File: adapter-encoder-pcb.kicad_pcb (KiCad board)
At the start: 4 copper layers, 14 x 15.6 mm, 33 parts, among them IC1 THVD2410VDRCR, M1 THRU_HOLE_PAD, M2 THRU_HOLE_PAD, U1 TLE5009E1000FUMA1, U2 STM32G031G6U6, U3 DF52-4S-0.8H(21), U4 SPX3819M5-L-3-3, U5 C2901617, U6 DF52-4S-0.8H(21), U7 SPX3819M5-L-3-3

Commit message: curves
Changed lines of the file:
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@@
   (segment (start 143.72885 110.81185) (end 144.098724 111.181724) (width 0.25) (layer "B.Cu") (net 22))
   (segment (start 143.727448 110.81185) (end 143.72885 110.81185) (width 0.25) (layer "B.Cu") (net 22))
-  (segment (start 145.304448 116.637448) (end 145.304448 116.350474) (width 0.3048) (layer "F.Cu") (net 23))
-  (segment (start 149.376423 115.340473) (end 150.864274 113.852622) (width 0.3048) (layer "F.Cu") (net 23))
+  (segment (start 150.529448 110.362448) (end 150.104448 110.362448) (width 0.3048) (layer "F.Cu") (net 23))
   (segment (start 144.504448 107.562448) (end 144.979108 108.037108) (width 0.3048) (layer "F.Cu") (net 23))
-  (segment (start 150.529448 110.362448) (end 150.104448 110.362448) (width 0.3048) (layer "F.Cu") (net 23))
   (segment (start 150.004448 110.262448) (end 150.104448 110.362448) (width 0.3048) (layer "F.Cu") (net 23))
+  (segment (start 145.490435 115.901461) (end 145.493461 115.898435) (width 0.3048) (layer "F.Cu") (net 23))
   (segment (start 145.942474 115.712448) (end 148.478397 115.712448) (width 0.3048) (layer "F.Cu") (net 23))
   (segment (start 144.979108 108.037108) (end 144.979108 108.760448) (width 0.3048) (layer "F.Cu") (net 23))
-  (segment (start 145.490435 115.901461) (end 145.493461 115.898435) (width 0.3048) (layer "F.Cu") (net 23))
   (segment (start 150.864273 110.697273) (end 150.529448 110.362448) (width 0.3048) (layer "F.Cu") (net 23))
   (segment (start 148.454448 110.437448) (end 149.279448 110.437448) (width 0.2032) (layer "F.Cu") (net 23))
   (segment (start 150.004448 109.712448) (end 150.004448 110.262448) (width 0.3048) (layer "F.Cu") (net 23))
+  (segment (start 149.376423 115.340473) (end 150.120325 114.596571) (width 0.3048) (layer "F.Cu") (net 23))
   (segment (start 144.504448 106.637448) (end 144.504448 107.562448) (width 0.3048) (layer "F.Cu") (net 23))
   (segment (start 149.279448 110.437448) (end 150.029448 110.437448) (width 0.2032) (layer "F.Cu") (net 23))
+  (segment (start 151.236248 111.902494) (end 151.236248 111.595299) (width 0.3048) (layer "F.Cu") (net 23))
+  (segment (start 145.304448 116.637448) (end 145.304448 116.350474) (width 0.3048) (layer "F.Cu") (net 23))
   (segment (start 150.029448 110.437448) (end 150.104448 110.362448) (width 0.2032) (layer "F.Cu") (net 23))
-  (segment (start 151.236248 112.954597) (end 151.236248 111.595299) (width 0.3048) (layer "F.Cu") (net 23))
   (via (at 144.979108 108.760448) (size 0.45) (drill 0.2) (layers "F.Cu" "B.Cu") (net 23))
   (via (at 150.004448 109.712448) (size 0.45) (drill 0.2) (layers "F.Cu" "B.Cu") (net 23))
-  (arc (start 145.490435 115.901461) (mid 145.352784 116.10747) (end 145.304448 116.350474) (width 0.3048) (layer "F.Cu") (net 23))
+  (arc (start 145.304448 116.350474) (mid 145.352784 116.10747) (end 145.490435 115.901461) (width 0.3048) (layer "F.Cu") (net 23))
+  (arc (start 145.493461 115.898435) (mid 145.69947 115.760784) (end 145.942474 115.712448) (width 0.3048) (layer "F.Cu") (net 23))
+  (arc (start 151.236248 111.902494) (mid 150.946229 113.360518) (end 150.120325 114.596571) (width 0.3048) (layer "F.Cu") (net 23))
   (arc (start 148.478397 115.712448) (mid 148.964405 115.615775) (end 149.376423 115.340473) (width 0.3048) (layer "F.Cu") (net 23))
-  (arc (start 150.864274 113.852622) (mid 151.139575 113.440605) (end 151.236248 112.954597) (width 0.3048) (layer "F.Cu") (net 23))
-  (arc (start 150.864273 110.697273) (mid 151.139575 111.109291) (end 151.236248 111.595299) (width 0.3048) (layer "F.Cu") (net 23))
-  (arc (start 145.493461 115.898435) (mid 145.69947 115.760784) (end 145.942474 115.712448) (width 0.3048) (layer "F.Cu") (net 23))
+  (arc (start 151.236248 111.595299) (mid 151.139575 111.109291) (end 150.864273 110.697273) (width 0.3048) (layer "F.Cu") (net 23))
   (segment (start 149.605499 109.712448) (end 150.004448 109.712448) (width 0.3048) (layer "In1.Cu") (net 23))
   (segment (start 144.979108 108.760448) (end 147.601397 108.760448) (width 0.3048) (layer "In1.Cu") (net 23))

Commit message: some minor tweaks
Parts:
- moved C6 0.20 mm to (146.5, 108.6)
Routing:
- net GND: vias 19 -> 31
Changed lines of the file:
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@@
   )
   (footprint "Capacitor_SMD:C_0402_1005Metric" (layer "F.Cu")
-    (at 146.304448 108.562448 180)
+    (at 146.504448 108.562448 180)
     (descr "Capacitor SMD 0402 (1005 Metric), square (rectangular) end terminal, IPC_7351 nominal, (Body size source: IPC-SM-782 page 76, https://www.pcb-3d.com/wordpress/wp-content/uploads/ipc-sm-782a_amendment_1_and_2.pdf), generated with kicad-footprint-generator")
     (tags "capacitor")
@@
     (stroke (width 0.0254) (type solid)) (layer "Edge.Cuts"))
   (via (at 150.608848 112.037448) (size 0.45) (drill 0.2) (layers "F.Cu" "B.Cu") (net 1))
+  (via (at 144.704448 104.737448) (size 0.45) (drill 0.2) (layers "F.Cu" "B.Cu") (net 1))
   (via (at 148.379448 116.987448) (size 0.45) (drill 0.2) (layers "F.Cu" "B.Cu") (net 1))
-  (via (at 141.279448 115.037448) (size 0.45) (drill 0.2) (layers "F.Cu" "B.Cu") (net 1))
+  (via (at 141.704448 114.737448) (size 0.45) (drill 0.2) (layers "F.Cu" "B.Cu") (net 1))
   (via (at 140.929448 114.637448) (size 0.45) (drill 0.2) (layers "F.Cu" "B.Cu") (net 1))
   (via (at 141.304448 110.337448) (size 0.45) (drill 0.2) (layers "F.Cu" "B.Cu") (net 1))
   (via (at 138.954448 109.687448) (size 0.45) (drill 0.2) (layers "F.Cu" "B.Cu") (net 1))
   (via (at 149.704448 115.937448) (size 0.45) (drill 0.2) (layers "F.Cu" "B.Cu") (net 1))
+  (via (at 145.804448 118.337448) (size 0.45) (drill 0.2) (layers "F.Cu" "B.Cu") (net 1))
+  (via (at 140.004448 107.337448) (size 0.45) (drill 0.2) (layers "F.Cu" "B.Cu") (net 1))
+  (via (at 142.304448 115.237448) (size 0.45) (drill 0.2) (layers "F.Cu" "B.Cu") (net 1))
   (via (at 149.454448 114.412448) (size 0.45) (drill 0.2) (layers "F.Cu" "B.Cu") (net 1))
   (via (at 145.004448 112.937448) (size 0.45) (drill 0.2) (layers "F.Cu" "B.Cu") (net 1))
+  (via (at 143.704448 118.337448) (size 0.45) (drill 0.2) (layers "F.Cu" "B.Cu") (net 1))
   (via (at 138.704448 114.012448) (size 0.45) (drill 0.2) (layers "F.Cu" "B.Cu") (net 1))
   (via (at 149.104448 112.837448) (size 0.45) (drill 0.2) (layers "F.Cu" "B.Cu") (net 1))
-  (via (at 148.554448 113.512448) (size 0.45) (drill 0.2) (layers "F.Cu" "B.Cu") (net 1))
+  (via (at 144.704448 118.837448) (size 0.45) (drill 0.2) (layers "F.Cu" "B.Cu") (net 1))
+  (via (at 150.404448 115.037448) (size 0.45) (drill 0.2) (layers "F.Cu" "B.Cu") (net 1))
+  (via (at 148.704448 113.437448) (size 0.45) (drill 0.2) (layers "F.Cu" "B.Cu") (net 1))
   (via (at 139.940347 109.669538) (size 0.45) (drill 0.2) (layers "F.Cu" "B.Cu") (net 1))
+  (via (at 145.904448 104.537448) (size 0.45) (drill 0.2) (layers "F.Cu" "B.Cu") (net 1))
   (via (at 142.354448 108.687448) (size 0.45) (drill 0.2) (layers "F.Cu" "B.Cu") (net 1))
+  (via (at 143.704448 104.637448) (size 0.45) (drill 0.2) (layers "F.Cu" "B.Cu") (net 1))
   (via (at 138.354448 112.387448) (size 0.45) (drill 0.2) (layers "F.Cu" "B.Cu") (net 1))
   (via (at 148.454448 106.087448) (size 0.45) (drill 0.2) (layers "F.Cu" "B.Cu") (net 1))
   (via (at 138.454448 110.037448) (size 0.45) (drill 0.2) (layers "F.Cu" "B.Cu") (net 1))
-  (via (at 138.454448 113.187448) (size 0.45) (drill 0.2) (layers "F.Cu" "B.Cu") (net 1))
+  (via (at 149.904448 107.537448) (size 0.45) (drill 0.2) (layers "F.Cu" "B.Cu") (net 1))
+  (via (at 138.604448 113.137448) (size 0.45) (drill 0.2) (layers "F.Cu" "B.Cu") (net 1))
+  (via (at 150.404448 113.237448) (size 0.45) (drill 0.2) (layers "F.Cu" "B.Cu") (net 1))
+  (via (at 151.204448 110.137448) (size 0.45) (drill 0.2) (layers "F.Cu" "B.Cu") (net 1))
   (via (at 143.579448 109.662448) (size 0.45) (drill 0.2) (layers "F.Cu" "B.Cu") (net 1))
   (segment (start 144.854448 112.287448) (end 144.404448 112.287448) (width 0.25) (layer "F.Cu") (net 2))
@@
   (segment (start 145.154448 109.937448) (end 145.654448 109.937448) (width 0.254) (layer "F.Cu") (net 12))
   (segment (start 143.204448 113.912448) (end 143.204448 113.837448) (width 0.381) (layer "F.Cu") (net 12))
+  (segment (start 145.654448 109.287448) (end 146.024448 108.917448) (width 0.254) (layer "F.Cu") (net 12))
   (segment (start 145.029448 109.812448) (end 145.154448 109.937448) (width 0.254) (layer "F.Cu") (net 12))
   (segment (start 139.354448 111.537448) (end 139.504448 111.687448) (width 0.381) (layer "F.Cu") (net 12))
@@
   (segment (start 142.629448 114.162448) (end 142.629448 113.054878) (width 0.25) (layer "F.Cu") (net 12))
   (segment (start 142.791948 114.324948) (end 143.204448 113.912448) (width 0.381) (layer "F.Cu") (net 12))
-  (segment (start 145.654448 109.937448) (end 145.654448 108.732448) (width 0.254) (layer "F.Cu") (net 12))
+  (segment (start 145.654448 109.937448) (end 145.654448 109.287448) (width 0.254) (layer "F.Cu") (net 12))
   (segment (start 142.429448 112.854878) (end 142.429448 112.812448) (width 0.25) (layer "F.Cu") (net 12))
-  (segment (start 145.654448 108.732448) (end 145.824448 108.562448) (width 0.254) (layer "F.Cu") (net 12))
   (segment (start 138.504448 111.537448) (end 139.354448 111.537448) (width 0.381) (layer "F.Cu") (net 12))
+  (segment (start 146.024448 108.917448) (end 146.024448 108.562448) (width 0.254) (layer "F.Cu") (net 12))
   (segment (start 141.954448 112.537448) (end 141.954448 111.837448) (width 0.25) (layer "F.Cu") (net 12))
   (segment (start 142.629448 113.054878) (end 142.429448 112.854878) (width 0.25) (layer "F.Cu") (net 12))
@@
   (segment (start 143.727448 110.81185) (end 143.72885 110.81185) (width 0.25) (layer "B.Cu") (net 22))
   (segment (start 150.529448 110.362448) (end 150.104448 110.362448) (width 0.3048) (layer "F.Cu") (net 23))
-  (segment (start 144.504448 107.562448) (end 144.979108 108.037108) (width 0.3048) (layer "F.Cu") (net 23))
   (segment (start 150.004448 110.262448) (end 150.104448 110.362448) (width 0.3048) (layer "F.Cu") (net 23))
   (segment (start 145.490435 115.901461) (end 145.493461 115.898435) (width 0.3048) (layer "F.Cu") (net 23))
+  (segment (start 145.204448 108.762237) (end 145.204448 108.262448) (width 0.3048) (layer "F.Cu") (net 23))
   (segment (start 145.942474 115.712448) (end 148.478397 115.712448) (width 0.3048) (layer "F.Cu") (net 23))
-  (segment (start 144.979108 108.037108) (end 144.979108 108.760448) (width 0.3048) (layer "F.Cu") (net 23))
   (segment (start 150.864273 110.697273) (end 150.529448 110.362448) (width 0.3048) (layer "F.Cu") (net 23))
   (segment (start 148.454448 110.437448) (end 149.279448 110.437448) (width 0.2032) (layer "F.Cu") (net 23))
   (segment (start 150.004448 109.712448) (end 150.004448 110.262448) (width 0.3048) (layer "F.Cu") (net 23))
   (segment (start 149.376423 115.340473) (end 150.120325 114.596571) (width 0.3048) (layer "F.Cu") (net 23))
-  (segment (start 144.504448 106.637448) (end 144.504448 107.562448) (width 0.3048) (layer "F.Cu") (net 23))
+  (segment (start 145.204448 108.262448) (end 144.504448 107.562448) (width 0.3048) (layer "F.Cu") (net 23))
   (segment (start 149.279448 110.437448) (end 150.029448 110.437448) (width 0.2032) (layer "F.Cu") (net 23))
   (segment (start 151.236248 111.902494) (end 151.236248 111.595299) (width 0.3048) (layer "F.Cu") (net 23))
+  (segment (start 144.504448 107.562448) (end 144.504448 106.637448) (width 0.3048) (layer "F.Cu") (net 23))
   (segment (start 145.304448 116.637448) (end 145.304448 116.350474) (width 0.3048) (layer "F.Cu") (net 23))
   (segment (start 150.029448 110.437448) (end 150.104448 110.362448) (width 0.2032) (layer "F.Cu") (net 23))
-  (via (at 144.979108 108.760448) (size 0.45) (drill 0.2) (layers "F.Cu" "B.Cu") (net 23))
+  (via (at 145.204448 108.762237) (size 0.45) (drill 0.2) (layers "F.Cu" "B.Cu") (net 23))
   (via (at 150.004448 109.712448) (size 0.45) (drill 0.2) (layers "F.Cu" "B.Cu") (net 23))
   (arc (start 145.304448 116.350474) (mid 145.352784 116.10747) (end 145.490435 115.901461) (width 0.3048) (layer "F.Cu") (net 23))
@@
   (arc (start 148.478397 115.712448) (mid 148.964405 115.615775) (end 149.376423 115.340473) (width 0.3048) (layer "F.Cu") (net 23))
   (arc (start 151.236248 111.595299) (mid 151.139575 111.109291) (end 150.864273 110.697273) (width 0.3048) (layer "F.Cu") (net 23))
+  (segment (start 145.204628 108.762057) (end 147.701221 108.762057) (width 0.3048) (layer "In1.Cu") (net 23))
+  (segment (start 148.499423 109.132423) (end 148.707474 109.340474) (width 0.3048) (layer "In1.Cu") (net 23))
   (segment (start 149.605499 109.712448) (end 150.004448 109.712448) (width 0.3048) (layer "In1.Cu") (net 23))
-  (segment (start 144.979108 108.760448) (end 147.601397 108.760448) (width 0.3048) (layer "In1.Cu") (net 23))
-  (segment (start 148.499423 109.132423) (end 148.707474 109.340474) (width 0.3048) (layer "In1.Cu") (net 23))
-  (arc (start 148.499423 109.132423) (mid 148.087405 108.857121) (end 147.601397 108.760448) (width 0.3048) (layer "In1.Cu") (net 23))
+  (segment (start 145.204448 108.762237) (end 145.204628 108.762057) (width 0.3048) (layer "In1.Cu") (net 23))
+  (arc (start 147.701221 108.762057) (mid 148.133098 108.877098) (end 148.499423 109.132423) (width 0.3048) (layer "In1.Cu") (net 23))
   (arc (start 148.707474 109.340474) (mid 149.119491 109.615775) (end 149.605499 109.712448) (width 0.3048) (layer "In1.Cu") (net 23))
   (segment (start 148.454448 110.937448) (end 149.104448 110.937448) (width 0.2032) (layer "F.Cu") (net 24))

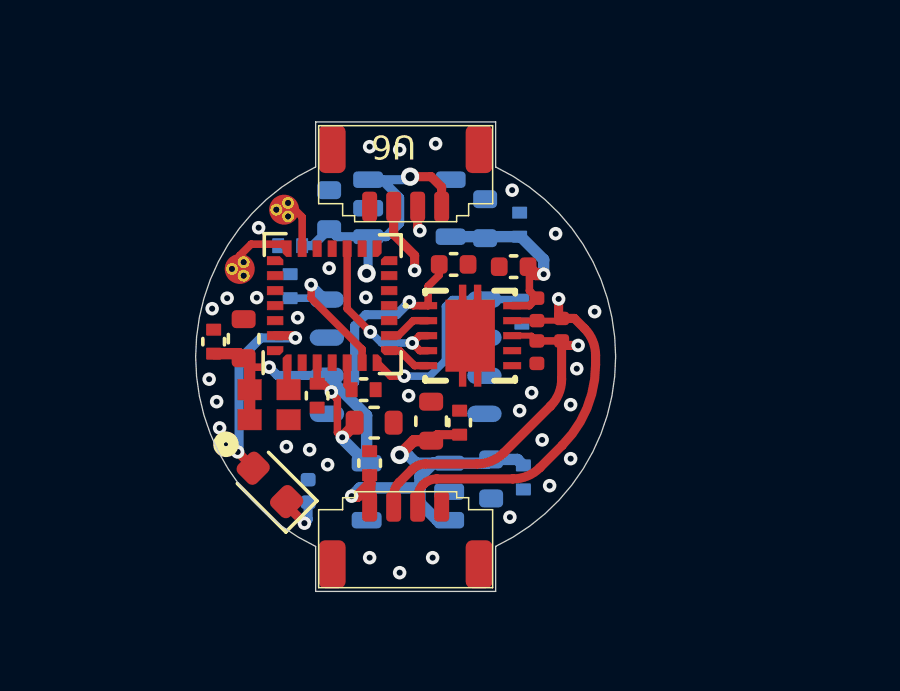
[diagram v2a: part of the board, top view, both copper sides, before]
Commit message: length matching rs485
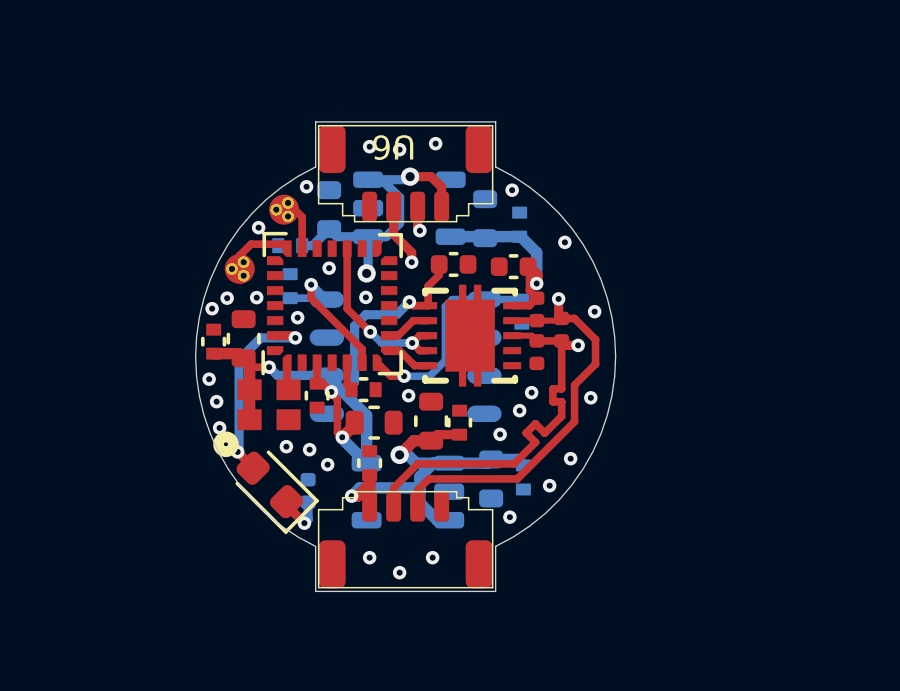
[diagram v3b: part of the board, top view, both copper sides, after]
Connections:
- net /A-PROTECTED renamed /RS485+
- net /B-PROTECTED renamed /RS485-
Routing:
- net /RS485+: track 20.6 -> 22.6 mm
- net /RS485-: track 20.9 -> 22.6 mm

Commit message: cad and silkscreen
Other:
- board text added: "CLK"
- board text added: "DIO"
- board text added: "GND"
- board text added: "VIN"
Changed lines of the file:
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@@
   (gr_line (start 141.90446 119.462127) (end 141.90446 117.962127)
     (stroke (width 0.0254) (type solid)) (layer "Edge.Cuts"))
+  (gr_text "DIO" (at 141.379448 107.337448) (layer "F.SilkS")
+    (effects (font (size 0.381 0.381) (thickness 0.0762) bold) (justify left bottom))
+  )
+  (gr_text "VIN" (at 141.429448 115.912448) (layer "F.SilkS")
+    (effects (font (size 0.635 0.635) (thickness 0.127) bold) (justify left bottom))
+  )
+  (gr_text "GND\n" (at 146.304448 115.912448) (layer "F.SilkS")
+    (effects (font (size 0.635 0.635) (thickness 0.127) bold) (justify left bottom))
+  )
+  (gr_text "CLK" (at 138.504448 109.887448) (layer "F.SilkS")
+    (effects (font (size 0.381 0.381) (thickness 0.0762) bold) (justify left bottom))
+  )
   (via (at 141.602448 105.973248) (size 0.45) (drill 0.2) (layers "F.Cu" "B.Cu") (net 1))
   (via (at 144.704448 104.737448) (size 0.45) (drill 0.2) (layers "F.Cu" "B.Cu") (net 1))
